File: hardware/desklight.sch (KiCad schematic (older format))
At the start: 9 parts, among them IC1 ATTINY10-TS, P1 AVR_TPI, P2 Pwr5V1500mA, P3 WS2812_CON, SW1 Rotary_Encoder_Switch

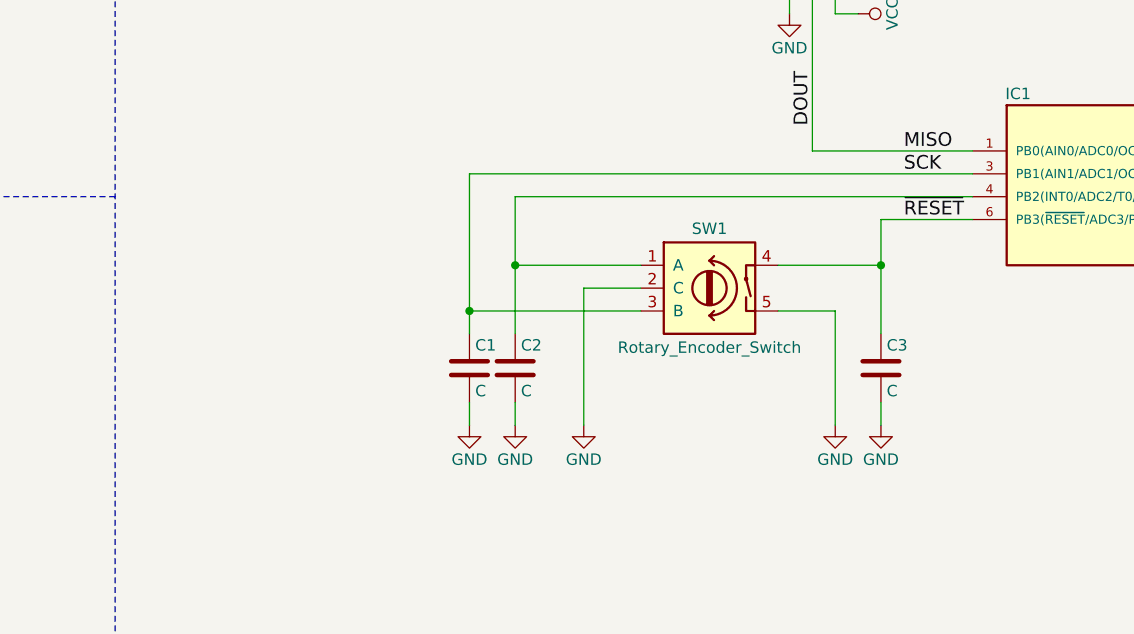
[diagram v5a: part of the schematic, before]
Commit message: added resistors to allow in-circuit programming
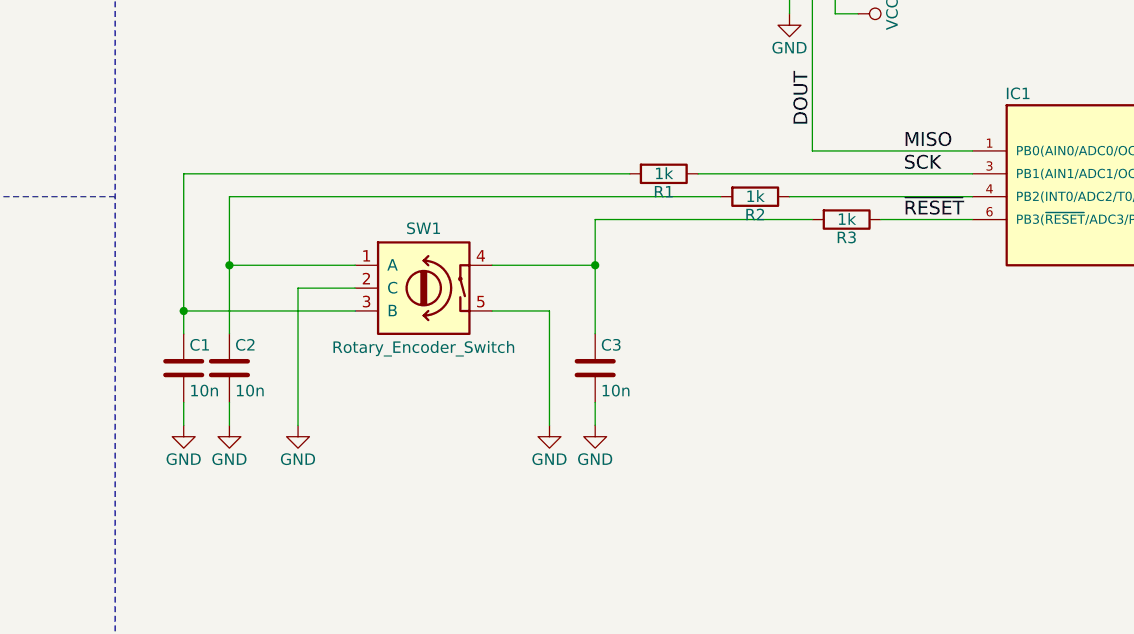
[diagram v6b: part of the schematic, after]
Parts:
- added R1, R2, R3: 1k, Resistors_SMD:R_0603_HandSoldering, symbol R
- C1, C2, C3: value C -> 10n
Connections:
- net SCK: now also R1.1; no longer C1.1, SW1.3 (B)
- net ~RESET: now also R3.1; no longer C3.1, SW1.4
- net at C2.1, SW1.1 (A): now also R2.2; no longer IC1.4 (PB2(INT0/ADC2/T0/PCINT2/CLKO))
- new net: IC1.4 (PB2(INT0/ADC2/T0/PCINT2/CLKO)), R2.1
- new net: C1.1, R1.2, SW1.3 (B)
- new net: C3.1, R3.2, SW1.4
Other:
- moved on the sheet: C1, C2, C3, SW1
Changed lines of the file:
@@
 L GND #PWR011
 U 1 1 588C1BAB
-P 6500 5000
-F 0 "#PWR011" H 6500 4750 50  0001 C CNN
-F 1 "GND" H 6500 4850 50  0000 C CNN
-F 2 "" H 6500 5000 50  0000 C CNN
-F 3 "" H 6500 5000 50  0000 C CNN
-	1    6500 5000
+P 5250 5000
+F 0 "#PWR011" H 5250 4750 50  0001 C CNN
+F 1 "GND" H 5250 4850 50  0000 C CNN
+F 2 "" H 5250 5000 50  0000 C CNN
+F 3 "" H 5250 5000 50  0000 C CNN
+	1    5250 5000
 	1    0    0    -1
 $EndComp
@@
 L Rotary_Encoder_Switch SW1
 U 1 1 58C9CC1D
-P 5950 4400
-F 0 "SW1" H 5950 4660 50  0000 C CNN
-F 1 "Rotary_Encoder_Switch" H 5950 4140 50  0000 C CNN
-F 2 "projectspecifics:Encoder_PEC11R" H 5850 4560 50  0001 C CNN
-F 3 "" H 5950 4660 50  0001 C CNN
-	1    5950 4400
+P 4700 4400
+F 0 "SW1" H 4700 4660 50  0000 C CNN
+F 1 "Rotary_Encoder_Switch" H 4700 4140 50  0000 C CNN
+F 2 "projectspecifics:Encoder_PEC11R" H 4600 4560 50  0001 C CNN
+F 3 "" H 4700 4660 50  0001 C CNN
+	1    4700 4400
 	1    0    0    -1
 $EndComp
@@
 L GND #PWR012
 U 1 1 58C9ECDB
-P 5400 5000
-F 0 "#PWR012" H 5400 4750 50  0001 C CNN
-F 1 "GND" H 5400 4850 50  0000 C CNN
-F 2 "" H 5400 5000 50  0000 C CNN
-F 3 "" H 5400 5000 50  0000 C CNN
-	1    5400 5000
+P 4150 5000
+F 0 "#PWR012" H 4150 4750 50  0001 C CNN
+F 1 "GND" H 4150 4850 50  0000 C CNN
+F 2 "" H 4150 5000 50  0000 C CNN
+F 3 "" H 4150 5000 50  0000 C CNN
+	1    4150 5000
 	1    0    0    -1
 $EndComp
@@
 L C C3
 U 1 1 596939D7
-P 6700 4750
-F 0 "C3" H 6725 4850 50  0000 L CNN
-F 1 "C" H 6725 4650 50  0000 L CNN
-F 2 "Capacitors_SMD:C_0603_HandSoldering" H 6738 4600 50  0001 C CNN
-F 3 "" H 6700 4750 50  0001 C CNN
-	1    6700 4750
-	1    0    0    -1
+P 5450 4750
+F 0 "C3" H 5475 4850 50  0000 L CNN
+F 1 "10n" H 5475 4650 50  0000 L CNN
+F 2 "Capacitors_SMD:C_0603_HandSoldering" H 5488 4600 50  0001 C CNN
+F 3 "" H 5450 4750 50  0001 C CNN
+	1    5450 4750
+	1    0    0    -1
+$EndComp
+$Comp
+L C C1
+U 1 1 59693BDB
+P 3650 4750
+F 0 "C1" H 3675 4850 50  0000 L CNN
+F 1 "10n" H 3675 4650 50  0000 L CNN
+F 2 "Capacitors_SMD:C_0603_HandSoldering" H 3688 4600 50  0001 C CNN
+F 3 "" H 3650 4750 50  0001 C CNN
+	1    3650 4750
+	1    0    0    -1
+$EndComp
+$Comp
+L C C2
+U 1 1 59693C1C
+P 3850 4750
+F 0 "C2" H 3875 4850 50  0000 L CNN
+F 1 "10n" H 3875 4650 50  0000 L CNN
+F 2 "Capacitors_SMD:C_0603_HandSoldering" H 3888 4600 50  0001 C CNN
+F 3 "" H 3850 4750 50  0001 C CNN
+	1    3850 4750
+	1    0    0    -1
+$EndComp
+$Comp
+L GND #PWR013
+U 1 1 59693D3B
+P 3850 5000
+F 0 "#PWR013" H 3850 4750 50  0001 C CNN
+F 1 "GND" H 3850 4850 50  0000 C CNN
+F 2 "" H 3850 5000 50  0001 C CNN
+F 3 "" H 3850 5000 50  0001 C CNN
+	1    3850 5000
+	1    0    0    -1
+$EndComp
+$Comp
+L GND #PWR014
+U 1 1 59693D61
+P 3650 5000
+F 0 "#PWR014" H 3650 4750 50  0001 C CNN
+F 1 "GND" H 3650 4850 50  0000 C CNN
+F 2 "" H 3650 5000 50  0001 C CNN
+F 3 "" H 3650 5000 50  0001 C CNN
+	1    3650 5000
+	1    0    0    -1
+$EndComp
+$Comp
+L GND #PWR015
+U 1 1 59693EE7
+P 5450 5000
+F 0 "#PWR015" H 5450 4750 50  0001 C CNN
+F 1 "GND" H 5450 4850 50  0000 C CNN
+F 2 "" H 5450 5000 50  0001 C CNN
+F 3 "" H 5450 5000 50  0001 C CNN
+	1    5450 5000
+	1    0    0    -1
+$EndComp
+$Comp
+L R R1
+U 1 1 5B296286
+P 5750 3900
+F 0 "R1" V 5830 3900 50  0000 C CNN
+F 1 "1k" V 5750 3900 50  0000 C CNN
+F 2 "Resistors_SMD:R_0603_HandSoldering" V 5680 3900 50  0001 C CNN
+F 3 "" H 5750 3900 50  0001 C CNN
+	1    5750 3900
+	0    1    1    0
+$EndComp
+$Comp
+L R R2
+U 1 1 5B2962E5
+P 6150 4000
+F 0 "R2" V 6230 4000 50  0000 C CNN
+F 1 "1k" V 6150 4000 50  0000 C CNN
+F 2 "Resistors_SMD:R_0603_HandSoldering" V 6080 4000 50  0001 C CNN
+F 3 "" H 6150 4000 50  0001 C CNN
+	1    6150 4000
+	0    1    1    0
+$EndComp
+$Comp
+L R R3
+U 1 1 5B296312
+P 6550 4100
+F 0 "R3" V 6630 4100 50  0000 C CNN
+F 1 "1k" V 6550 4100 50  0000 C CNN
+F 2 "Resistors_SMD:R_0603_HandSoldering" V 6480 4100 50  0001 C CNN
+F 3 "" H 6550 4100 50  0001 C CNN
+	1    6550 4100
+	0    1    1    0
 $EndComp
 Wire Wire Line
@@
 Wire Wire Line
 	1700 6100 1400 6100
-Wire Wire Line
-	6700 4100 7100 4100
 Wire Wire Line
 	6300 3100 6300 3200
@@
 	1250 2300 1900 2300
 Wire Wire Line
-	6250 4500 6500 4500
-Wire Wire Line
-	6250 4300 6700 4300
-Wire Wire Line
-	4900 3900 7100 3900
-Wire Wire Line
-	7100 4000 5100 4000
-Wire Wire Line
-	5100 4300 5650 4300
-Wire Wire Line
-	4900 4500 5650 4500
-Wire Wire Line
-	5650 4400 5400 4400
-Wire Wire Line
-	5400 4400 5400 5000
-Wire Wire Line
-	6700 4100 6700 4600
-Wire Wire Line
-	5100 4000 5100 4600
-Wire Wire Line
-	4900 3900 4900 4600
+	5000 4500 5250 4500
+Wire Wire Line
+	5000 4300 5450 4300
+Wire Wire Line
+	3850 4300 4400 4300
+Wire Wire Line
+	3650 4500 4400 4500
+Wire Wire Line
+	4400 4400 4150 4400
+Wire Wire Line
+	4150 4400 4150 5000
+Wire Wire Line
+	5450 4100 5450 4600
+Wire Wire Line
+	3850 4000 3850 4600
+Wire Wire Line
+	3650 3900 3650 4600
 Connection ~ 1600 2200
 Connection ~ 1600 2300
-Connection ~ 6700 4300
-Wire Wire Line
-	6500 4500 6500 5000
-$Comp
-L C C1
-U 1 1 59693BDB
-P 4900 4750
-F 0 "C1" H 4925 4850 50  0000 L CNN
-F 1 "C" H 4925 4650 50  0000 L CNN
-F 2 "Capacitors_SMD:C_0603_HandSoldering" H 4938 4600 50  0001 C CNN
-F 3 "" H 4900 4750 50  0001 C CNN
-	1    4900 4750
-	1    0    0    -1
-$EndComp
-$Comp
-L C C2
-U 1 1 59693C1C
-P 5100 4750
-F 0 "C2" H 5125 4850 50  0000 L CNN
-F 1 "C" H 5125 4650 50  0000 L CNN
-F 2 "Capacitors_SMD:C_0603_HandSoldering" H 5138 4600 50  0001 C CNN
-F 3 "" H 5100 4750 50  0001 C CNN
-	1    5100 4750
-	1    0    0    -1
-$EndComp
-Connection ~ 5100 4300
-Connection ~ 4900 4500
-Wire Wire Line
-	4900 4900 4900 5000
-Wire Wire Line
-	5100 4900 5100 5000
-$Comp
-L GND #PWR013
-U 1 1 59693D3B
-P 5100 5000
-F 0 "#PWR013" H 5100 4750 50  0001 C CNN
-F 1 "GND" H 5100 4850 50  0000 C CNN
-F 2 "" H 5100 5000 50  0001 C CNN
-F 3 "" H 5100 5000 50  0001 C CNN
-	1    5100 5000
-	1    0    0    -1
-$EndComp
-$Comp
-L GND #PWR014
-U 1 1 59693D61
-P 4900 5000
-F 0 "#PWR014" H 4900 4750 50  0001 C CNN
-F 1 "GND" H 4900 4850 50  0000 C CNN
-F 2 "" H 4900 5000 50  0001 C CNN
-F 3 "" H 4900 5000 50  0001 C CNN
-	1    4900 5000
-	1    0    0    -1
-$EndComp
-Wire Wire Line
-	6700 4900 6700 5000
-$Comp
-L GND #PWR015
-U 1 1 59693EE7
-P 6700 5000
-F 0 "#PWR015" H 6700 4750 50  0001 C CNN
-F 1 "GND" H 6700 4850 50  0000 C CNN
-F 2 "" H 6700 5000 50  0001 C CNN
-F 3 "" H 6700 5000 50  0001 C CNN
-	1    6700 5000
-	1    0    0    -1
-$EndComp
+Connection ~ 5450 4300
+Wire Wire Line
+	5250 4500 5250 5000
+Connection ~ 3850 4300
+Connection ~ 3650 4500
+Wire Wire Line
+	3650 4900 3650 5000
+Wire Wire Line
+	3850 4900 3850 5000
+Wire Wire Line
+	5450 4900 5450 5000
+Wire Wire Line
+	5450 4100 6400 4100
+Wire Wire Line
+	6700 4100 7100 4100
+Wire Wire Line
+	3850 4000 6000 4000
+Wire Wire Line
+	6300 4000 7100 4000
+Wire Wire Line
+	3650 3900 5600 3900
+Wire Wire Line
+	5900 3900 7100 3900
 $EndSCHEMATC

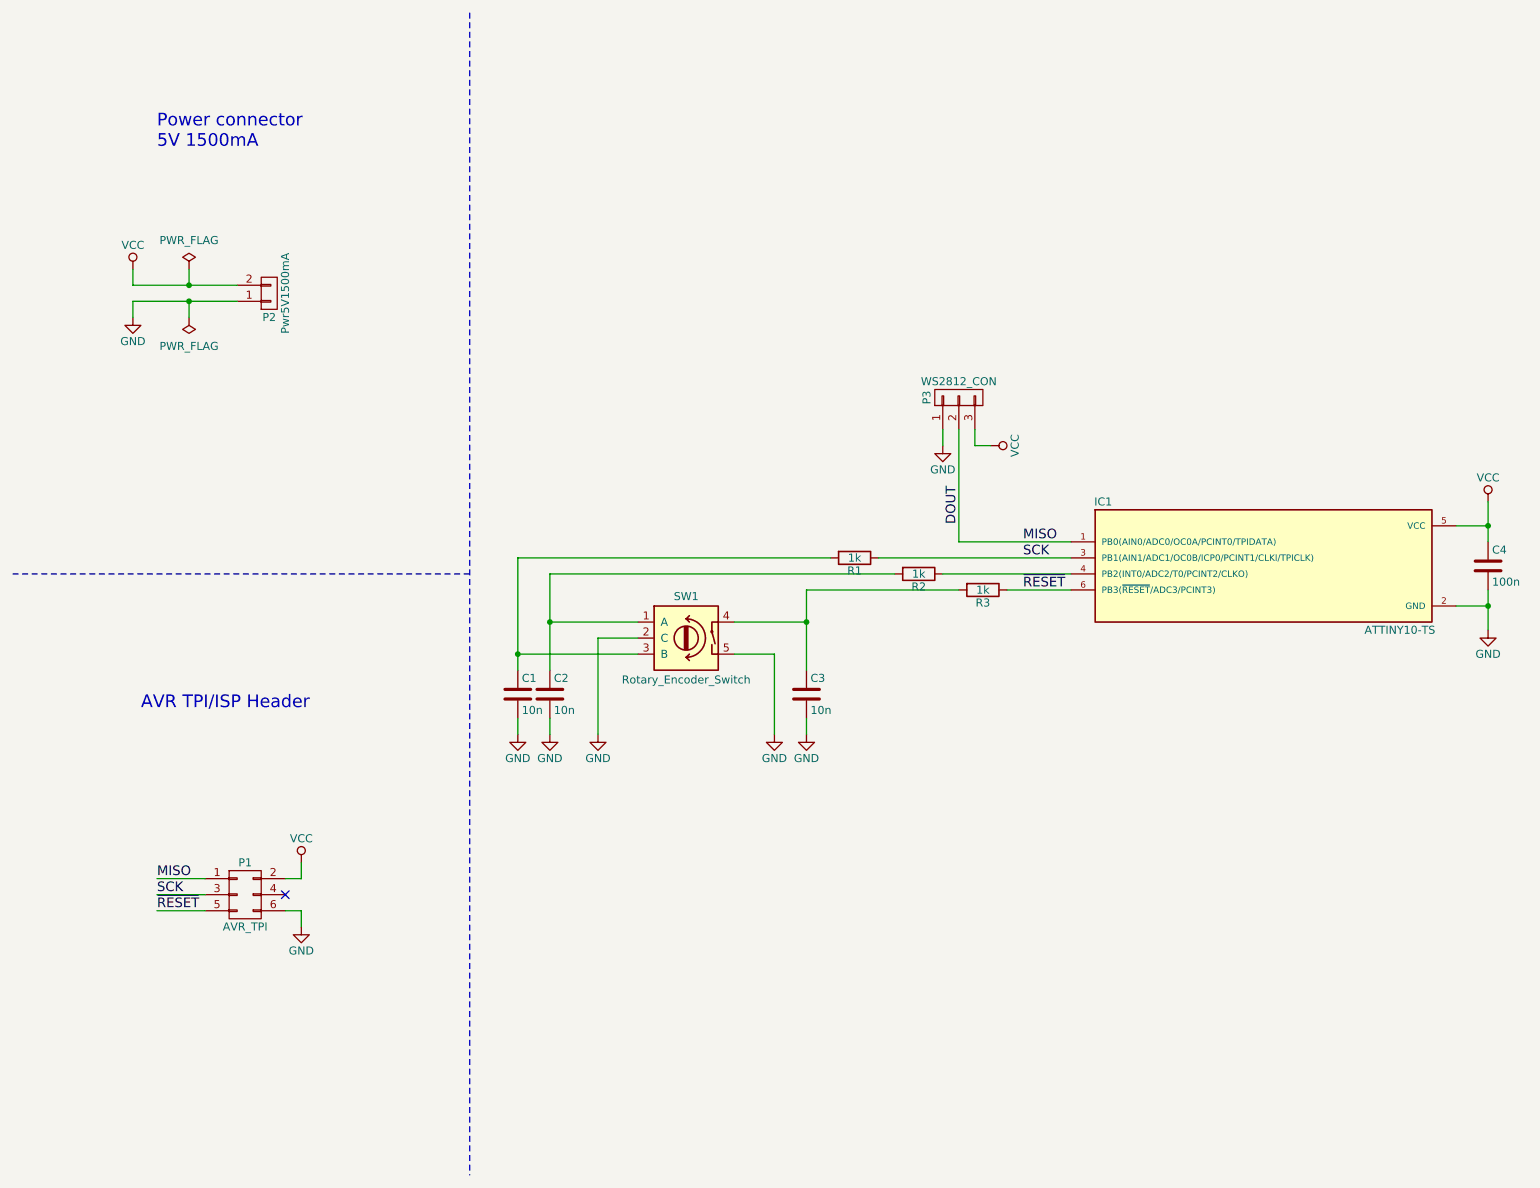
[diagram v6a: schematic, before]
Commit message: PCB version 1.0, also panelized in 10x10cm and production-ready zip file for upload to your favourite PCB store.
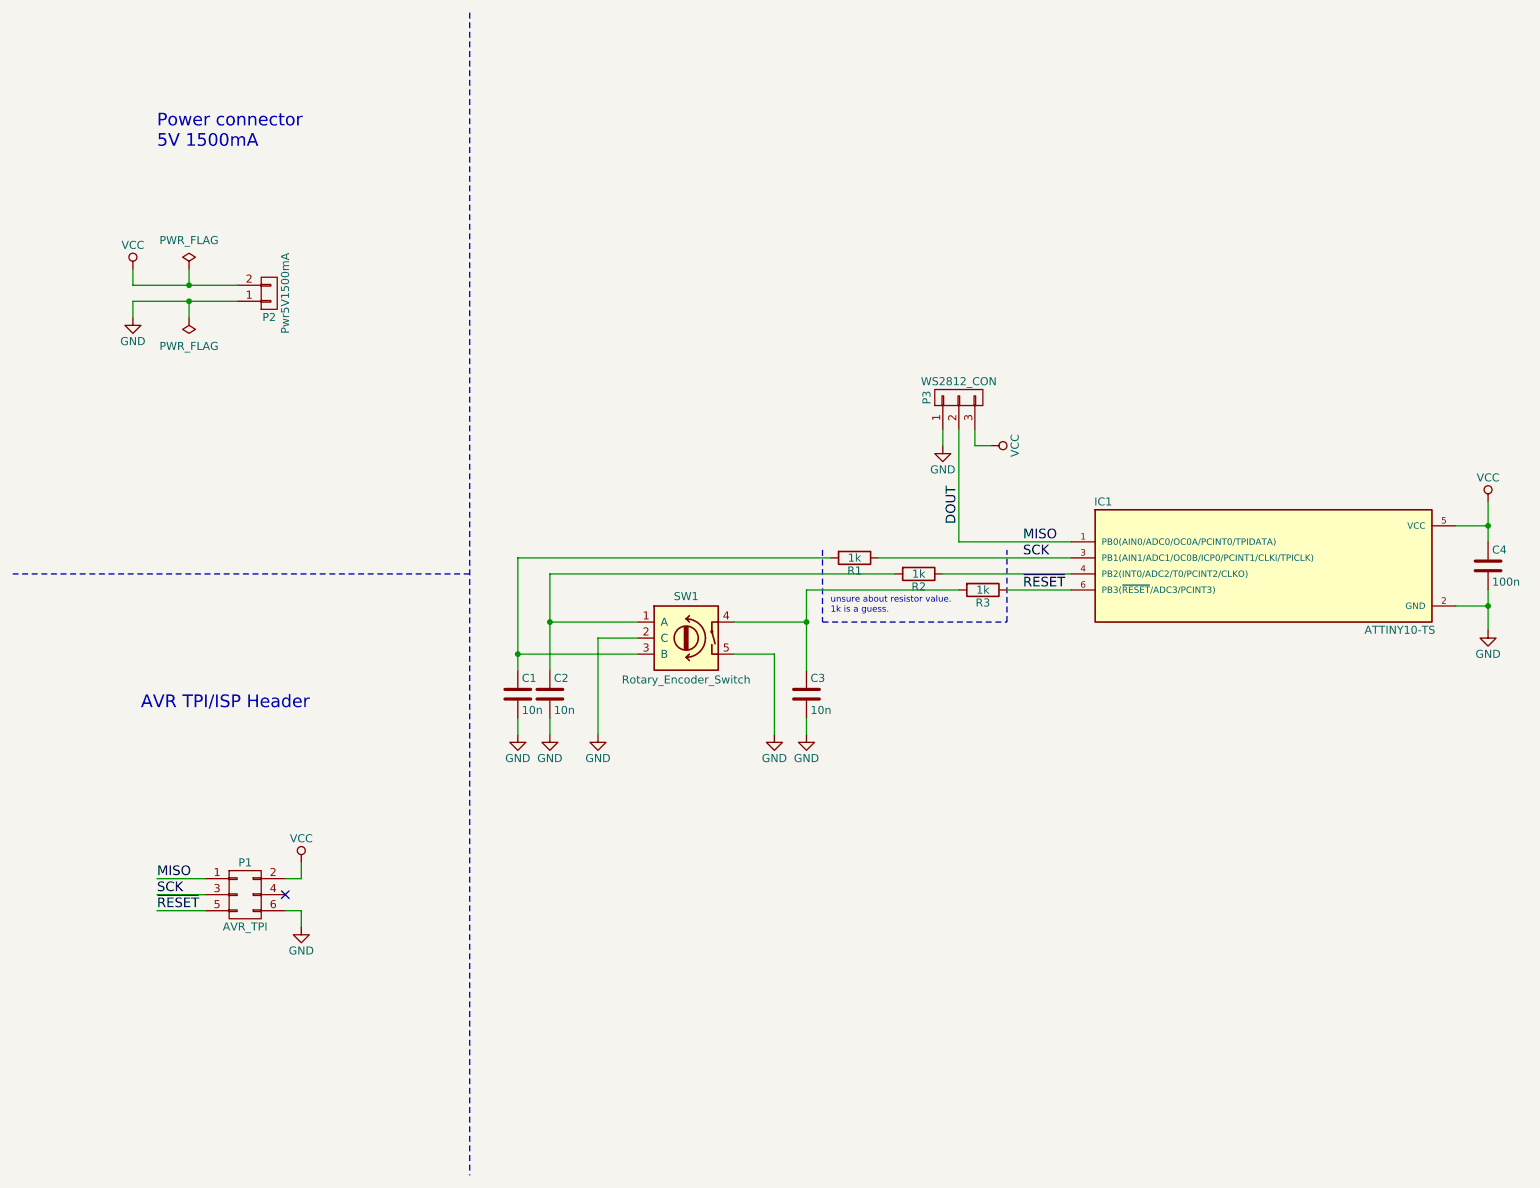
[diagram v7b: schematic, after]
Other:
- note added: "unsure about resistor value.\n1k is a guess."
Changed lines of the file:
@@
 encoding utf-8
 Sheet 1 1
-Title "WS2812-based desktop lamp"
-Date "2017-01-28"
-Rev ""
+Title "tiny-ws2812-desklight"
+Date "2018-06-19"
+Rev "v1.0"
 Comp ""
-Comment1 "David R. Piegdon"
-Comment2 "<dgit@piegdon.de>"
-Comment3 ""
-Comment4 ""
+Comment1 "<dgit@piegdon.de>"
+Comment2 "David R. Piegdon"
+Comment3 "github.com/dpiegdon/tiny-ws2812-desklight"
+Comment4 "WS2812-based desktop lamp"
 $EndDescr
 $Comp
@@
 	9500 3700 9700 3700
 Wire Wire Line
-	9700 3550 9700 3800
-Wire Wire Line
-	9700 4100 9700 4350
+	9700 3550 9700 3700
+Wire Wire Line
+	9700 3700 9700 3800
+Wire Wire Line
+	9700 4100 9700 4200
+Wire Wire Line
+	9700 4200 9700 4350
 Wire Wire Line
 	9700 4200 9500 4200
@@
 	1600 2100 1600 2200
 Wire Wire Line
-	1250 2200 1900 2200
-Wire Wire Line
-	1250 2300 1900 2300
+	1250 2200 1600 2200
+Wire Wire Line
+	1600 2200 1900 2200
+Wire Wire Line
+	1250 2300 1600 2300
+Wire Wire Line
+	1600 2300 1900 2300
 Wire Wire Line
 	5000 4500 5250 4500
@@
 	4150 4400 4150 5000
 Wire Wire Line
-	5450 4100 5450 4600
-Wire Wire Line
-	3850 4000 3850 4600
-Wire Wire Line
-	3650 3900 3650 4600
+	5450 4100 5450 4300
+Wire Wire Line
+	5450 4300 5450 4600
+Wire Wire Line
+	3850 4000 3850 4300
+Wire Wire Line
+	3850 4300 3850 4600
+Wire Wire Line
+	3650 3900 3650 4500
+Wire Wire Line
+	3650 4500 3650 4600
 Connection ~ 1600 2200
 Connection ~ 1600 2300
@@
 Wire Wire Line
 	5900 3900 7100 3900
+Wire Notes Line
+	5550 3850 5550 4300
+Wire Notes Line
+	5550 4300 6700 4300
+Wire Notes Line
+	6700 4300 6700 3850
+Text Notes 5600 4250 0    39   ~ 0
+unsure about resistor value.\n1k is a guess.
 $EndSCHEMATC

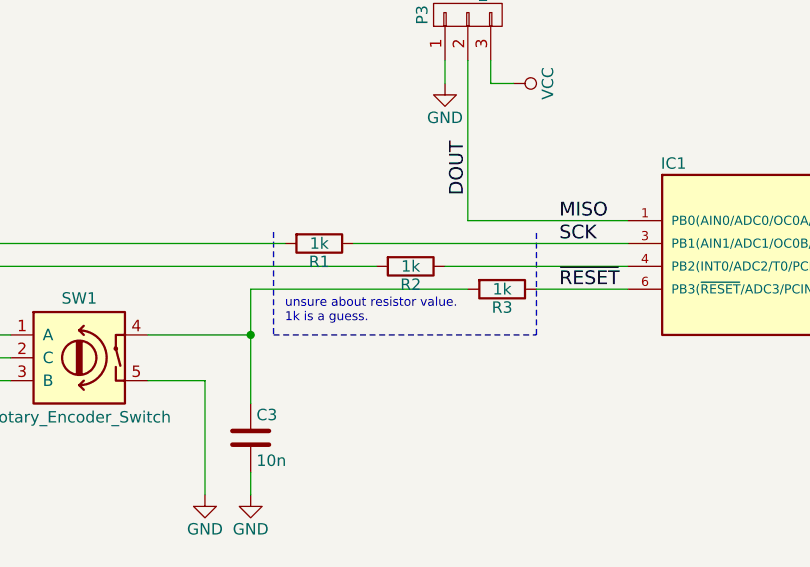
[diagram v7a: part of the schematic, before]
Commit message: schematic: 1K resistors seem fine
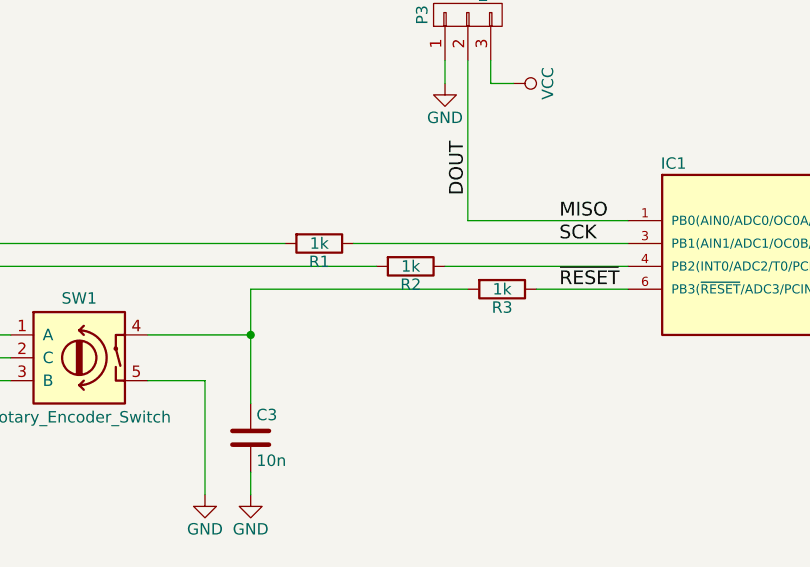
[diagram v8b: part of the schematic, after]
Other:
- note removed: "unsure about resistor value.\n1k is a guess."
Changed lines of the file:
@@
 Wire Wire Line
 	5900 3900 7100 3900
-Wire Notes Line
-	5550 3850 5550 4300
-Wire Notes Line
-	5550 4300 6700 4300
-Wire Notes Line
-	6700 4300 6700 3850
-Text Notes 5600 4250 0    39   ~ 0
-unsure about resistor value.\n1k is a guess.
 $EndSCHEMATC
